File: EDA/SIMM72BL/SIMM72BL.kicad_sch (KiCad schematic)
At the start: 59 parts, among them J1 5822021-4, U1 SIMM-72, U10 74HC14, U7 74HC14, U8 74HC14, U9 74HC14

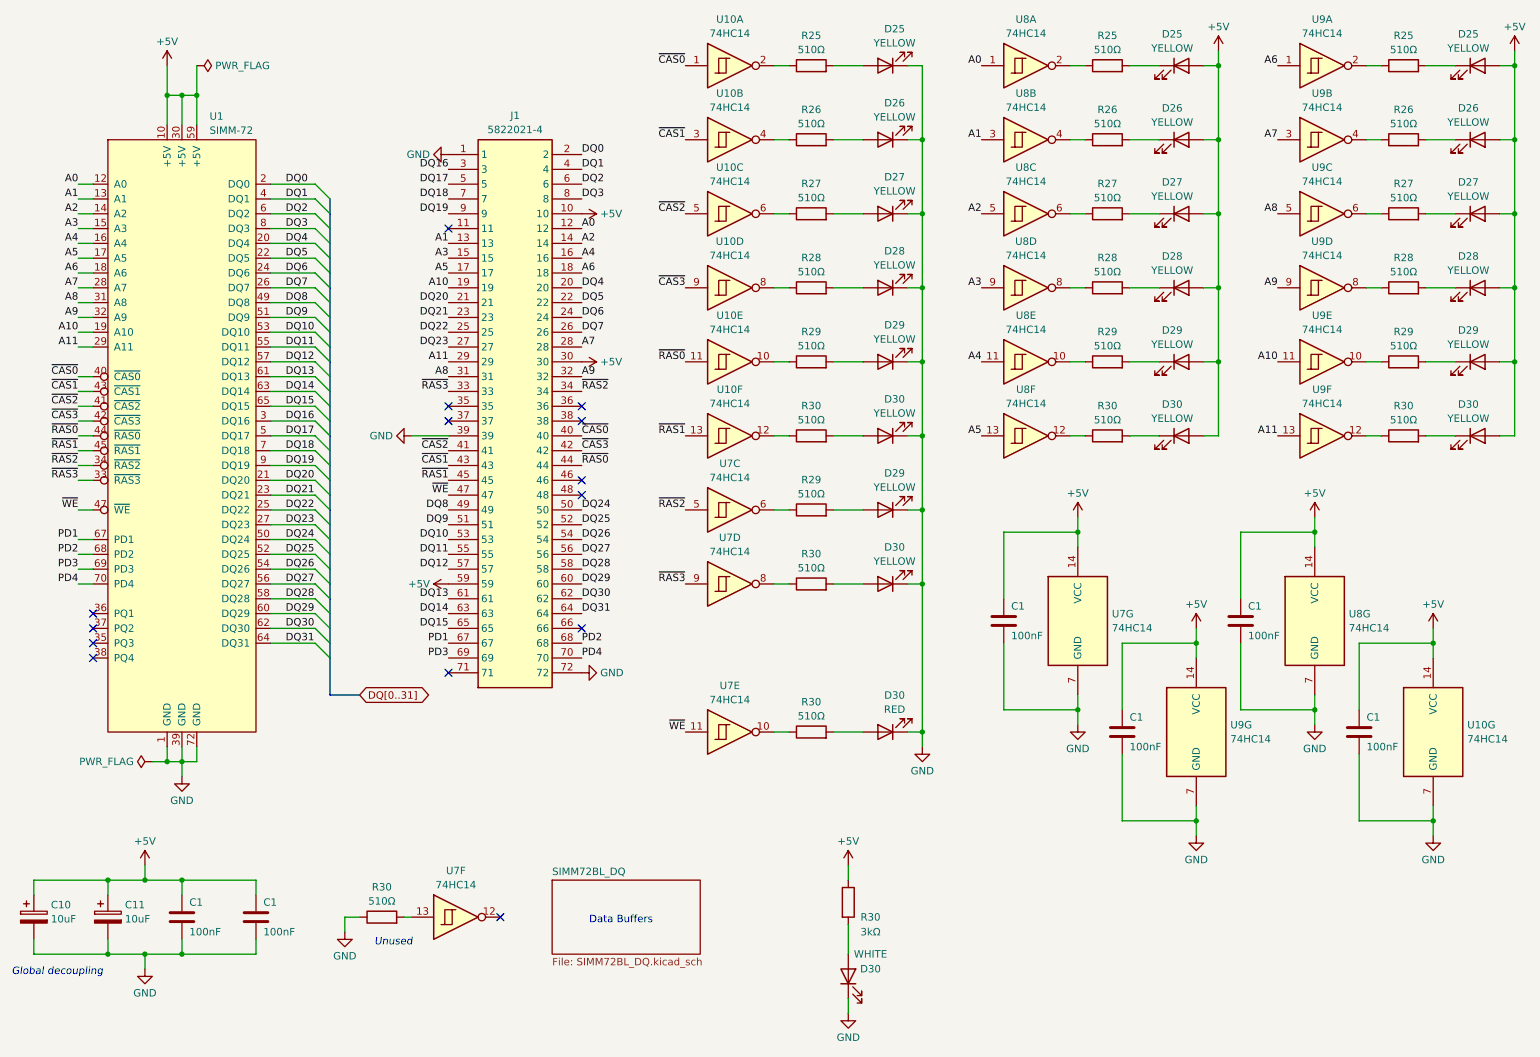
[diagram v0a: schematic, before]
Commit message: SIMM72BL v1.2: fixed decoupling caps footprint & silkscreen
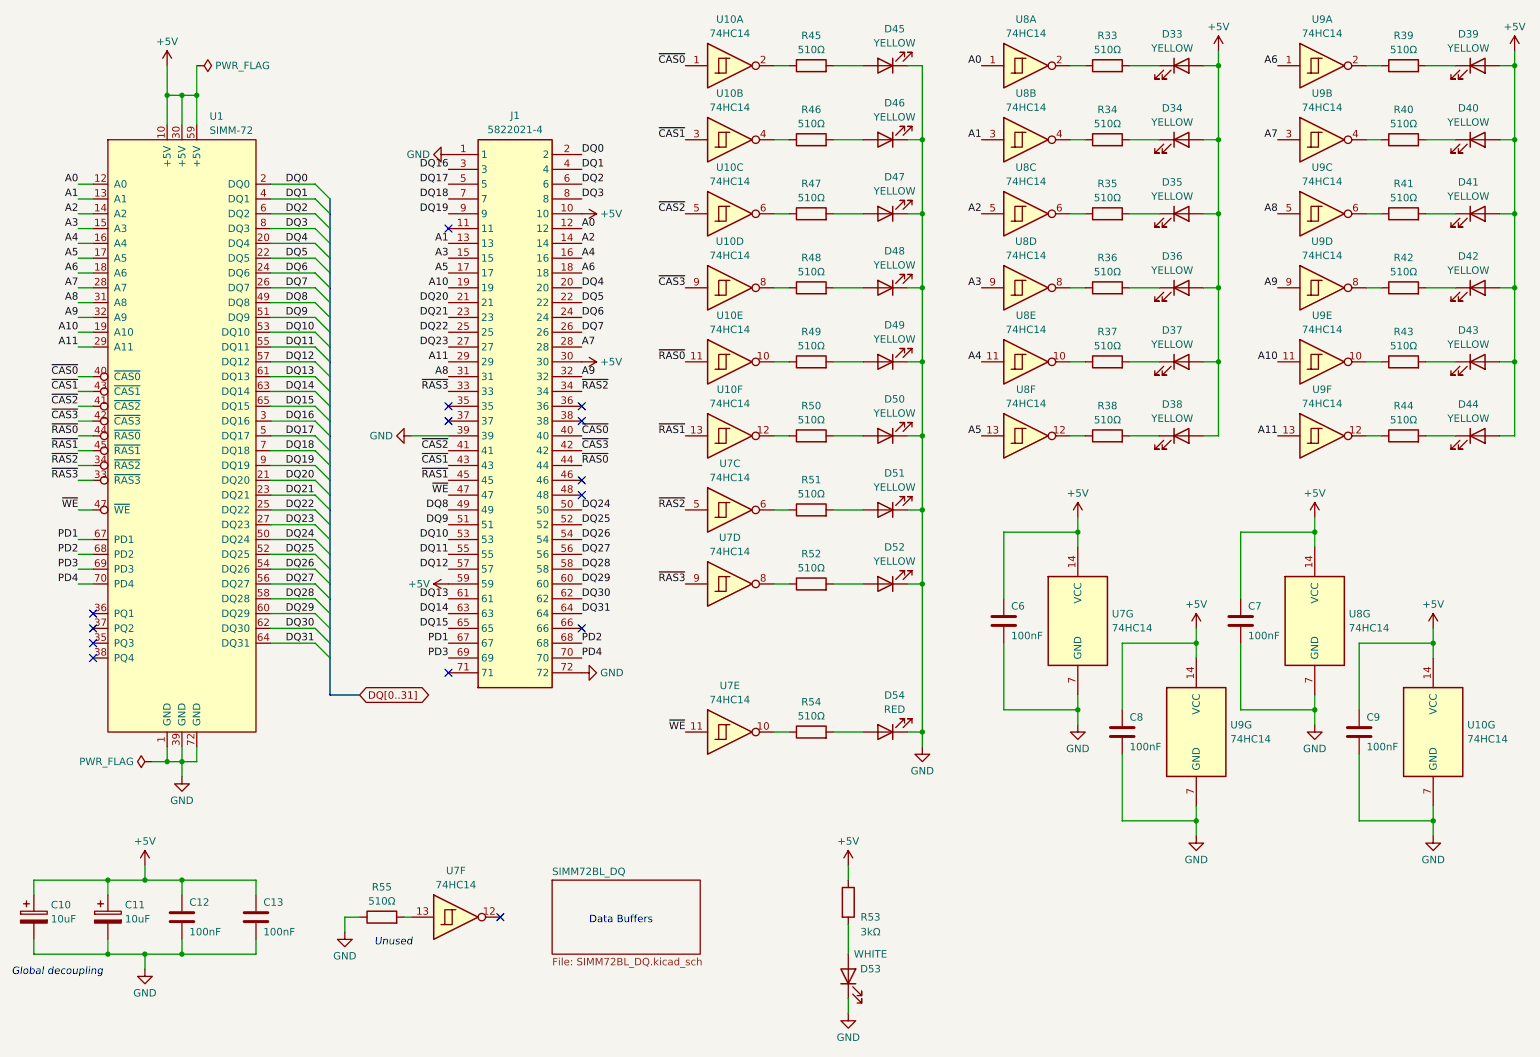
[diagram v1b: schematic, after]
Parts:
- renumbered C1 to C12, C1 to C13, C1 to C6, C1 to C7, C1 to C8, C1 to C9, D25 to D33, D26 to D34, D27 to D35, D28 to D36, D29 to D37, D30 to D38, D25 to D39, D26 to D40, D27 to D41, D28 to D42, D29 to D43, D30 to D44, D25 to D45, D26 to D46, D27 to D47, D28 to D48, D29 to D49, D30 to D50, D29 to D51, D30 to D52, D30 to D53, D30 to D54, R25 to R33, R26 to R34, R27 to R35, R28 to R36, R29 to R37, R30 to R38, R25 to R39, R26 to R40, R27 to R41, R28 to R42, R29 to R43, R30 to R44, R25 to R45, R26 to R46, R27 to R47, R28 to R48, R29 to R49, R30 to R50, R29 to R51, R30 to R52, R30 to R53, R30 to R54, R30 to R55
